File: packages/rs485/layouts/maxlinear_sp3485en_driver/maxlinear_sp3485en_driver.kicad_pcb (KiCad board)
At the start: 2 copper layers, 3 parts

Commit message: Rebuild all
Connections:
- net hv renamed VCC
- net line renamed DI
- net line-1 renamed RO
- net line-2 renamed A
- net line-3 renamed B
- U1 pad 2: line-4 -> REh
- U1 pad 3: line-4 -> DE
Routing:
- net (no net): track 0.00 -> 9.77 mm
- net line-4: track 3.89 -> 0.00 mm
- net B: track 1.99 -> 0.00 mm
- net A: track 1.96 -> 0.00 mm
- net VCC: track 1.93 -> 0.00 mm

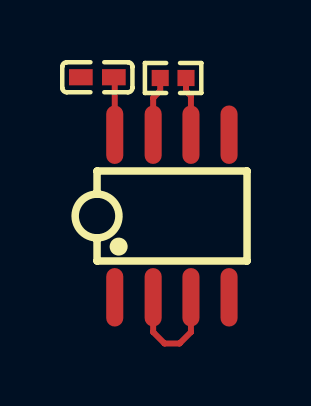
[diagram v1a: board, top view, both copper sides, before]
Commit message: Fix LDO power in voltage range
Fix RS485 sp3485 and is2092 RE WE connections
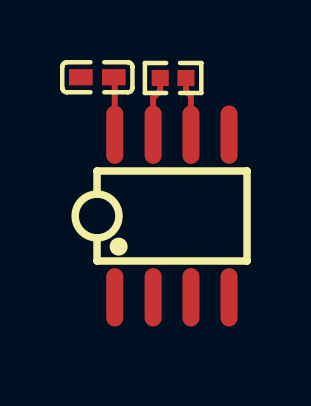
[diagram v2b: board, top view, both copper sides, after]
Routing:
- net (no net): track 9.77 -> 0.00 mm
- net B: track 0.00 -> 1.99 mm
- net A: track 0.00 -> 1.96 mm
- net VCC: track 0.00 -> 1.93 mm

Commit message: WIP update rs485
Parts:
- C1: footprint atopile:C0402-b3ef17 -> Samsung_Electro_Mechanics_CL05B104KO5NNNC:C0402
- R1: footprint atopile:R0402-56259e -> FH_RC_02K1200FT:R0402
- U1: footprint atopile:SOIC-8_L5.0-W4.0-P1.27-LS6.0-BL-294f77 -> MaxLinear_SP3485EN_L_TR:SOIC-8_L5.0-W4.0-P1.27-LS6.0-BL

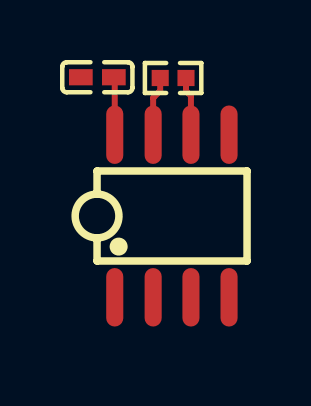
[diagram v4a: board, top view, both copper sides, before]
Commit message: Update 3D model locations
fix missing renders
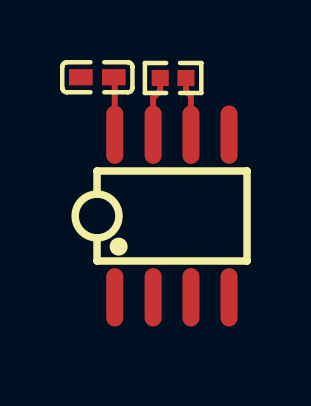
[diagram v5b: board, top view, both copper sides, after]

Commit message: rebuild all packages & regenerate images of changed layouts (silk)
Add new scripts for version bump and build (based on atopile/packages)
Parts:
- R1: footprint FH_RC_02K1200FT:R0402 -> UNI_ROYAL_0402WGF1200TCE:R0402
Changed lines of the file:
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@@
         )
     )
-    (footprint "FH_RC_02K1200FT:R0402"
+    (footprint "UNI_ROYAL_0402WGF1200TCE:R0402"
         (layer "F.Cu")
         (at 0.035005 -4.6 180)
@@
             )
         )
-        (property "Datasheet" "https://www.lcsc.com/datasheet/lcsc_datasheet_2304140030_FH--Guangdong-Fenghua-Advanced-Tech-RC-02K1200FT_C140206.pdf"
+        (property "Datasheet" "https://www.lcsc.com/datasheet/lcsc_datasheet_2205311900_UNI-ROYAL-Uniroyal-Elec-0402WGF1200TCE_C25079.pdf"
             (at 0 0 0)
             (layer "F.Fab")
@@
             )
         )
-        (property "__atopile_lib_fp_hash__" "57cbe434-22b7-9f1a-d98e-d9d7e3424886"
-            (at 0 0 0)
-            (layer "User.9")
-            (hide yes)
-            (effects
-                (font
-                    (size 0.125 0.125)
-                    (thickness 0.01875)
-                )
-            )
-        )
-        (property "LCSC" "C140206"
-            (at 0 0 0)
-            (layer "User.9")
-            (hide yes)
-            (effects
-                (font
-                    (size 0.125 0.125)
-                    (thickness 0.01875)
-                )
-            )
-        )
-        (property "Partnumber" "RC-02K1200FT"
-            (at 0 0 0)
-            (layer "User.9")
-            (hide yes)
-            (effects
-                (font
-                    (size 0.125 0.125)
-                    (thickness 0.01875)
-                )
-            )
-        )
-        (property "Manufacturer" "FH(Guangdong Fenghua Advanced Tech)"
+        (property "__atopile_lib_fp_hash__" "012ff7eb-db55-6667-4901-ff32deef5046"
+            (at 0 0 0)
+            (layer "User.9")
+            (hide yes)
+            (effects
+                (font
+                    (size 0.125 0.125)
+                    (thickness 0.01875)
+                )
+            )
+        )
+        (property "LCSC" "C25079"
+            (at 0 0 0)
+            (layer "User.9")
+            (hide yes)
+            (effects
+                (font
+                    (size 0.125 0.125)
+                    (thickness 0.01875)
+                )
+            )
+        )
+        (property "Partnumber" "0402WGF1200TCE"
+            (at 0 0 0)
+            (layer "User.9")
+            (hide yes)
+            (effects
+                (font
+                    (size 0.125 0.125)
+                    (thickness 0.01875)
+                )
+            )
+        )
+        (property "Manufacturer" "UNI-ROYAL(Uniroyal Elec)"
             (at 0 0 0)
             (layer "User.9")
@@
             )
         )
-        (property "checksum" "faebd9e285ec905981839fe28718e5d5046b5d2c3056accddbe92b06ba806f3b"
-            (at 0 0 0)
-            (layer "User.9")
-            (hide yes)
-            (effects
-                (font
-                    (size 0.125 0.125)
-                    (thickness 0.01875)
-                )
+        (property "checksum" "01018d9f05719ca2a94d85e3da5e0e10c32908b2642ac0c2bb2c8ffaf62ecc76"
+            (at 0 0 0)
+            (layer "User.9")
+            (hide no)
+            (effects
+                (font
+                    (size 0.125 0.125)
+                    (thickness 0.01875)
+                )
+                (hide yes)
             )
         )
         (attr smd)
+        (fp_line
+            (start -0.23 0.5)
+            (end -0.94 0.5)
+            (stroke
+                (width 0.15)
+                (type solid)
+            )
+            (layer "F.SilkS")
+        )
+        (fp_line
+            (start -0.94 0.5)
+            (end -0.94 -0.5)
+            (stroke
+                (width 0.15)
+                (type solid)
+            )
+            (layer "F.SilkS")
+        )
+        (fp_line
+            (start -0.94 -0.5)
+            (end -0.23 -0.5)
+            (stroke
+                (width 0.15)
+                (type solid)
+            )
+            (layer "F.SilkS")
+        )
+        (fp_line
+            (start 0.23 0.5)
+            (end 0.94 0.5)
+            (stroke
+                (width 0.15)
+                (type solid)
+            )
+            (layer "F.SilkS")
+        )
         (fp_line
             (start 0.94 0.5)
@@
             (start 0.94 -0.5)
             (end 0.23 -0.5)
-            (stroke
-                (width 0.15)
-                (type solid)
-            )
-            (layer "F.SilkS")
-        )
-        (fp_line
-            (start 0.23 0.5)
-            (end 0.94 0.5)
-            (stroke
-                (width 0.15)
-                (type solid)
-            )
-            (layer "F.SilkS")
-        )
-        (fp_line
-            (start -0.23 0.5)
-            (end -0.94 0.5)
-            (stroke
-                (width 0.15)
-                (type solid)
-            )
-            (layer "F.SilkS")
-        )
-        (fp_line
-            (start -0.94 0.5)
-            (end -0.94 -0.5)
-            (stroke
-                (width 0.15)
-                (type solid)
-            )
-            (layer "F.SilkS")
-        )
-        (fp_line
-            (start -0.94 -0.5)
-            (end -0.23 -0.5)
             (stroke
                 (width 0.15)
@@
             (layer "F.Fab")
         )
+        (fp_text user "%R"
+            (at 0 0 0)
+            (layer "F.Fab")
+            (effects
+                (font
+                    (size 1 1)
+                    (thickness 0.15)
+                )
+            )
+            (unlocked no)
+        )
         (fp_text user "${REFERENCE}"
-            (at 0 0 0)
-            (layer "F.Fab")
+            (at 0 -4 0)
+            (layer "F.SilkS")
             (effects
                 (font
@@
             )
             (unlocked no)
+        )
+        (pad "2" smd rect
+            (at 0.43 0 180)
+            (size 0.57 0.54)
+            (layers "F.Cu" "F.Paste" "F.Mask")
+            (net 1 "B")
         )
         (pad "1" smd rect
             (at -0.43 0 180)
             (size 0.57 0.54)
-            (layers "F.Cu" "F.Mask" "F.Paste")
+            (layers "F.Cu" "F.Paste" "F.Mask")
             (net 7 "A")
         )
-        (pad "2" smd rect
-            (at 0.43 0 180)
-            (size 0.57 0.54)
-            (layers "F.Cu" "F.Mask" "F.Paste")
-            (net 1 "B")
-        )
-        (embedded_fonts no)
-        (model "${KIPRJMOD}/../../parts/FH_RC_02K1200FT/R0402_L1.0-W0.5-H0.4.step"
+        (model "${KIPRJMOD}/../../parts/UNI_ROYAL_0402WGF1200TCE/R0402_L1.0-W0.5-H0.4.step"
             (offset
                 (xyz 0 0 0)

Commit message: fix rs485 frozen build
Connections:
- net REh renamed nRE
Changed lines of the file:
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@@
     (net 4 "gnd")
     (net 5 "DI")
-    (net 6 "REh")
+    (net 6 "nRE")
     (net 7 "A")
     (net 8 "VCC")
@@
             (size 0.57 1.95)
             (layers "F.Cu" "F.Mask" "F.Paste")
-            (net 6 "REh")
+            (net 6 "nRE")
         )
         (pad "3" smd oval
